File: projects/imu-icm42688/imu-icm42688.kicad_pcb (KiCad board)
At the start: 2 copper layers, 20 x 15 mm, 14 parts, among them J1 HEADER, U1 AP2112K-3.3, U2 ICM-42688-P

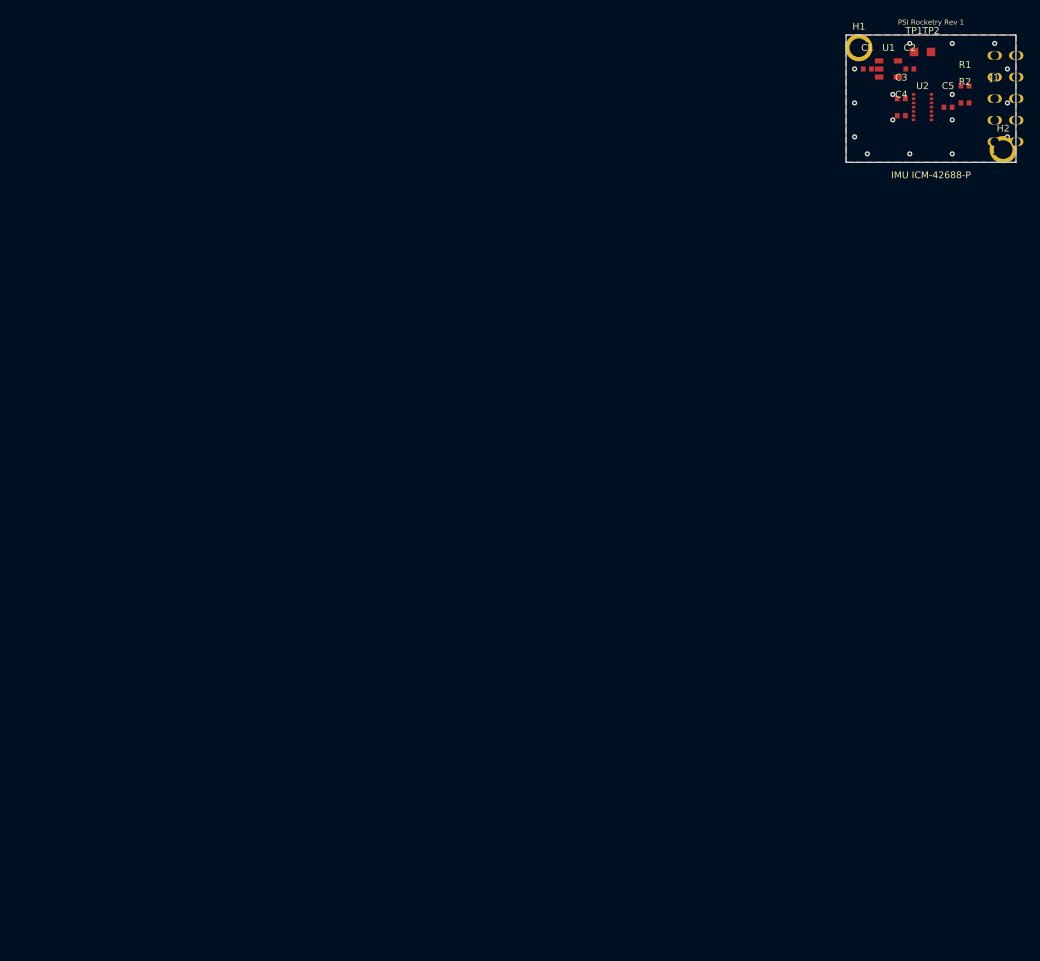
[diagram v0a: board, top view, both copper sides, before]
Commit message: PCB workspace: scoped escape hatch, hardened gates, repo cleanup
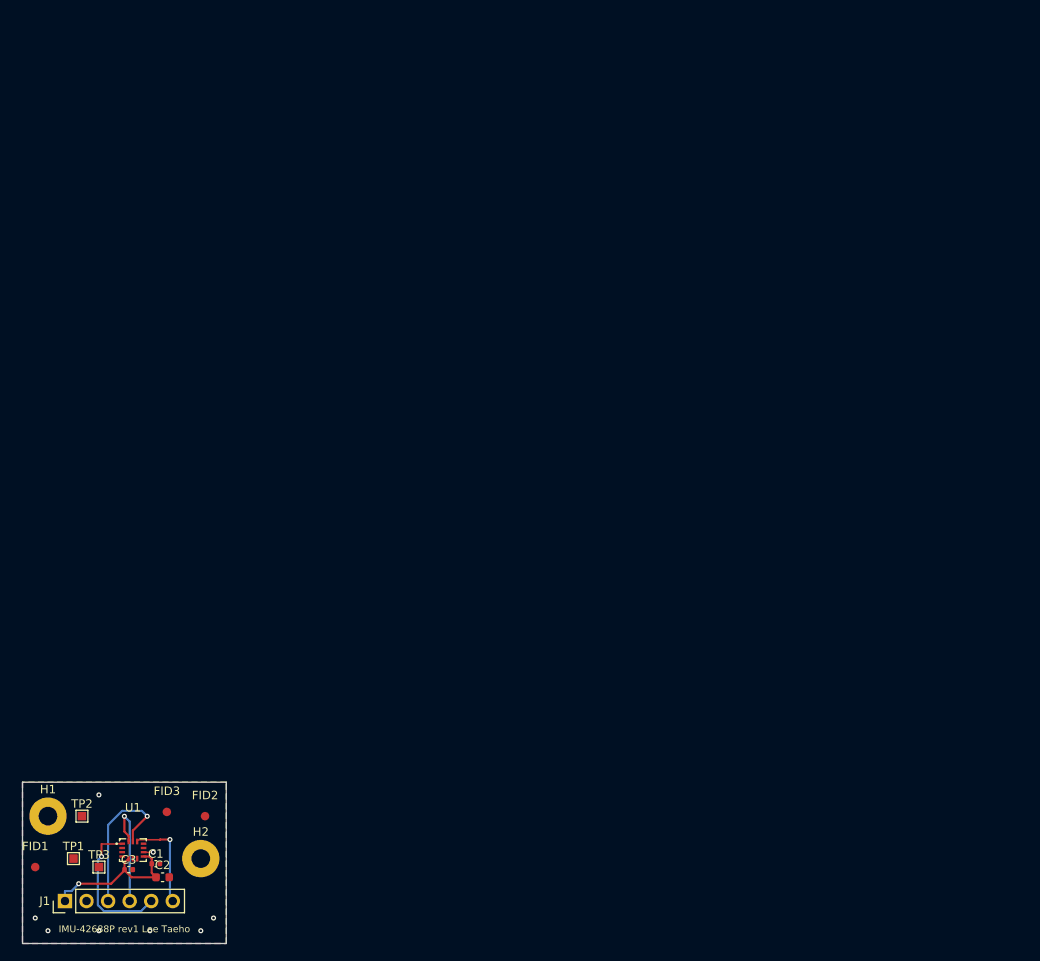
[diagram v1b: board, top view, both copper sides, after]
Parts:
- removed C4: 100nF, Capacitor_SMD:C_0402_1005Metric
- removed C5: 1uF, Capacitor_SMD:C_0402_1005Metric
- removed R1, R2: 4.7k, Resistor_SMD:R_0402_1005Metric
- removed U2: ICM-42688-P, Package_LGA:LGA-14_2.5x3mm
- added FID1: FIDUCIAL, Fiducial:Fiducial_1mm_Mask3mm, F.Cu at (4.50, 198.0)
- added FID2: FIDUCIAL, Fiducial:Fiducial_1mm_Mask3mm, F.Cu at (24.5, 192.0)
- added FID3: FIDUCIAL, Fiducial:Fiducial_1mm_Mask3mm, F.Cu at (20.0, 191.5)
- added TP3: INT1, TestPoint:TestPoint_Pad_1.0x1.0mm, F.Cu at (12.0, 198.0)
- C1: value 1uF -> 100nF
- C2: value 1uF -> 2.2uF; footprint Capacitor_SMD:C_0402_1005Metric -> Capacitor_SMD:C_0603_1608Metric
- C3: value 100nF -> 10nF
- H1, H2: value MH -> M2
- J1: value HEADER -> SPI-HDR; footprint Connector_PinHeader_2.54mm:PinHeader_2x05_P2.54mm_Vertical -> Connector_PinHeader_2.54mm:PinHeader_1x06_P2.54mm_Vertical
- TP1: value 3V3 -> +3V3
- U1: value AP2112K-3.3 -> ICM-42688-P; footprint Package_TO_SOT_SMD:SOT-23-5 -> jlcpcb:LGA-14_L3.0-W2.5-P0.50-TL
- moved J1 144.6 mm to (8.00, 202.0), turned to 90 degrees
- moved TP1 137.2 mm to (9.00, 197.0)
- moved TP2 134.5 mm to (10.0, 192.0)
- moved H1 131.6 mm to (6.00, 192.0)
- moved C2 129.6 mm to (19.5, 199.2)
- moved C3 128.6 mm to (15.5, 198.3)
- moved U1 128.0 mm to (16.0, 196.0)
- moved H2 126.1 mm to (24.0, 197.0)
- moved C1 125.6 mm to (18.7, 197.6)
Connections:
- C1 pad 1: VIN -> +3V3
- H1 pad 1: GND -> (no net)
- H2 pad 1: GND -> (no net)
- J1 pad 1: VIN -> +3V3
- J1 pad 2: +3V3 -> GND
- J1 pad 3: SCL_SCLK -> SPI_SCLK
- J1 pad 4: SDA_SDI -> SPI_SDI
- J1 pad 5: SDO -> SPI_SDO
- J1 pad 6: nCS -> SPI_CS
- TP1 pad 1: +3V3 -> (no net)
- TP2 pad 1: GND -> (no net)
- U1 pad 1: VIN -> SPI_SDO
- U1 pad 2: GND -> (no net)
- U1 pad 4: (no net) -> INT1
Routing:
- net +3V3: track 0.00 -> 18.3 mm, vias 0 -> 1
- net SPI_SCLK: track 0.00 -> 18.2 mm, vias 0 -> 1
- net SPI_SDO: track 0.00 -> 16.9 mm, vias 0 -> 1
- net SPI_SDI: track 0.00 -> 13.4 mm, vias 0 -> 1
- net SPI_CS: track 0.00 -> 11.4 mm, vias 0 -> 1
- net GND: track 0.00 -> 1.14 mm, vias 18 -> 8
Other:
- board size 20 x 15 mm -> 24 x 19 mm
- rule pad_to_mask_clearance: 0.05 -> 0
- board text added: "IMU-42688P rev1 Lee Taeho"
- board text removed: "IMU ICM-42688-P"
- board text removed: "PSI Rocketry Rev 1"

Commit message: 9/6 update
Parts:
- moved FID3 20.5 mm to (5.00, 205.5)
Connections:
- TP1 pad 1: (no net) -> +3V3
- TP2 pad 1: (no net) -> GND
- TP3 pad 1: (no net) -> INT1
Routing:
- net SPI_SCLK: track 18.2 -> 10.7 mm
- net +3V3: track 18.3 -> 21.8 mm, vias 1 -> 0
- net INT1: track 0.00 -> 3.26 mm
- net SPI_SDO: track 16.9 -> 14.6 mm
- net SPI_SDI: track 13.4 -> 15.7 mm
- net GND: track 1.14 -> 2.72 mm, vias 8 -> 11
- net SPI_CS: track 11.4 -> 10.9 mm, vias 1 -> 0

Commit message: batch
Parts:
- moved FID3 19.8 mm to (24.8, 204.9)
- moved FID1 1.00 mm to (5.10, 197.2)
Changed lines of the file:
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@@
 	(footprint "Fiducial:Fiducial_1mm_Mask3mm"
 		(layer "F.Cu")
-		(at 5 205.5)
+		(at 24.8 204.9)
 		(descr "Fiducial, circular marking, 1mm bare copper, 3mm soldermask opening (recommended)")
 		(tags "fiducial")
 		(property "Reference" "FID3"
-			(at 0 -2.45 0)
-			(layer "F.SilkS")
-			(effects
-				(font
-					(size 1 1)
-					(thickness 0.15)
+			(at -0.3 -2.5 0)
+			(layer "F.SilkS")
+			(effects
+				(font
+					(size 0.8 0.8)
+					(thickness 0.12)
 				)
 			)
@@
 	(footprint "Fiducial:Fiducial_1mm_Mask3mm"
 		(layer "F.Cu")
-		(at 4.5 198)
+		(at 5.1 197.2)
 		(descr "Fiducial, circular marking, 1mm bare copper, 3mm soldermask opening (recommended)")
 		(tags "fiducial")
 		(property "Reference" "FID1"
-			(at 0 -2.45 0)
-			(layer "F.SilkS")
-			(effects
-				(font
-					(size 1 1)
-					(thickness 0.15)
+			(at 0 2.3 0)
+			(layer "F.SilkS")
+			(effects
+				(font
+					(size 0.8 0.8)
+					(thickness 0.12)
 				)
 			)
@@
 		(tags "capacitor")
 		(property "Reference" "C2"
-			(at 0 -1.43 0)
-			(layer "F.SilkS")
-			(effects
-				(font
-					(size 1 1)
-					(thickness 0.15)
+			(at 2.5 0 0)
+			(layer "F.SilkS")
+			(effects
+				(font
+					(size 0.8 0.8)
+					(thickness 0.12)
 				)
 			)
@@
 		(tags "capacitor")
 		(property "Reference" "C3"
-			(at 0 -1.16 0)
-			(layer "F.SilkS")
-			(effects
-				(font
-					(size 1 1)
-					(thickness 0.15)
+			(at 0 1.1 0)
+			(layer "F.SilkS")
+			(effects
+				(font
+					(size 0.8 0.8)
+					(thickness 0.12)
 				)
 			)
@@
 		)
 		(pad "1" thru_hole rect
-			(at 0 0)
+			(at 0 0 90)
 			(size 1.7 1.7)
 			(drill 1)
@@
 		)
 		(pad "2" thru_hole circle
-			(at 0 2.54)
+			(at 0 2.54 90)
 			(size 1.7 1.7)
 			(drill 1)
@@
 		)
 		(pad "3" thru_hole circle
-			(at 0 5.08)
+			(at 0 5.08 90)
 			(size 1.7 1.7)
 			(drill 1)
@@
 		)
 		(pad "4" thru_hole circle
-			(at 0 7.62)
+			(at 0 7.62 90)
 			(size 1.7 1.7)
 			(drill 1)
@@
 		)
 		(pad "5" thru_hole circle
-			(at 0 10.16)
+			(at 0 10.16 90)
 			(size 1.7 1.7)
 			(drill 1)
@@
 		)
 		(pad "6" thru_hole circle
-			(at 0 12.7)
+			(at 0 12.7 90)
 			(size 1.7 1.7)
 			(drill 1)
@@
 		(layer "Edge.Cuts")
 	)
-	(gr_text "IMU-42688P rev1 Lee Taeho"
-		(at 15 205.3 0)
+	(gr_text "IMU-42688P rev1\nLee Taeho"
+		(at 15 205.2 0)
 		(layer "F.SilkS")
 		(effects
@@
 	)
 	(via
-		(at 4.5 204)
+		(at 4.5 202)
 		(size 0.6)
 		(drill 0.3)
@@
 	)
 	(via
-		(at 24 205.5)
+		(at 21.5 205.5)
 		(size 0.6)
 		(drill 0.3)
@@
 	)
 	(via
-		(at 6 205.5)
+		(at 7.5 205.5)
 		(size 0.6)
 		(drill 0.3)
@@
 	)
 	(via
-		(at 25.5 204)
+		(at 25.5 201.5)
 		(size 0.6)
 		(drill 0.3)
